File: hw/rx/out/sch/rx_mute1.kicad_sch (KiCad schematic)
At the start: 10 parts, among them Q1 BSS138, U7 TPS3808G01

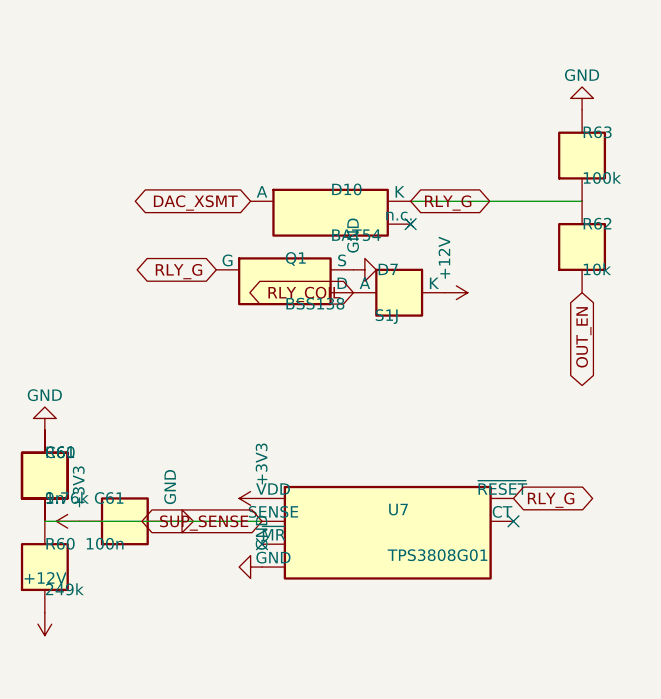
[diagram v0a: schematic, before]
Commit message: hw/rx: receiver module BT40NE -> BT40E, FEM node pack-only (ADR-0021, #112)
- hw/rx: BT40E symbol (Fanstel v1.09 p.14 pad map = BT40F/NE names), footprint
  openpack:Fanstel_BT40E (14x16 mm), no FEM nets, P1.05 open; GPIO map unchanged.
  ERC 0/0. BOM: Digi-Key UK GBP 9.7765 q100 -> $30.68 / GBP 23.38 per sub-board.
- fw: receiver builds add boards/role_rx_cpunet.overlay (FEM node disabled, no
  &radio fem); rx.c refuses to build with the FEM enabled.
- ADR-0014 amended (datasheet checks, FCC X8WBT40F, no UKCA DoC, BOM).

Co-Authored-By: Claude Opus 5.5 <noreply@anthropic.com>
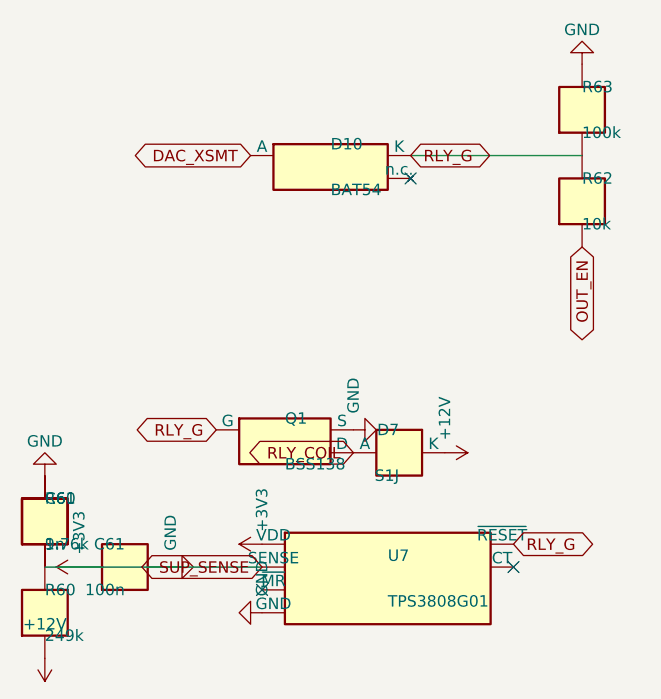
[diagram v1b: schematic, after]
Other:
- moved on the sheet: C60, C61, D10, D7, Q1, R60, R61, R62, R63, U7

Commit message: hw/rx: receiver sub-board layout, 50 ohm GCPW, keyed J1, JLC rules that load, fab outputs (#34) (#116)
Part of #34. Receiver layout (48x90 mm, DRC 0/0), #116 independent-review fixes (netclass pour clearances in rx + pack, no hole at J1 pin 14, solid RF grounds, K1 pin-1/CPL), every placed part with a checked LCSC code.

Co-Authored-By: Claude Opus 5.5 <noreply@anthropic.com>
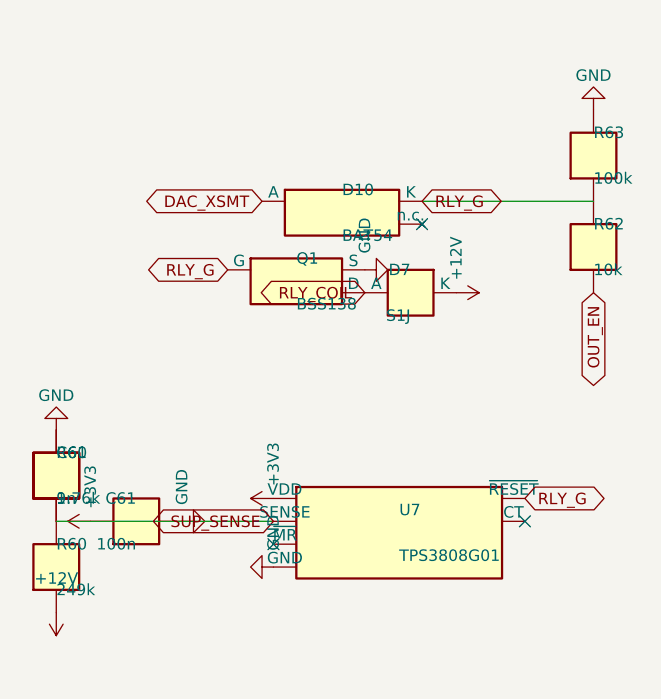
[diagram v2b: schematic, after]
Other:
- moved on the sheet: C60, C61, D10, D7, Q1, R60, R61, R62, R63, U7
